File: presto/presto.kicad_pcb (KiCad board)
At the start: 2 copper layers, 27 parts, among them J1 Conn_01x03_Pin, J10 Conn_01x03_Pin, J11 Conn_01x03_Socket, J12 Conn_01x03_Socket, J13 Conn_01x03_Socket, J14 Conn_01x03_Socket, J15 Conn_01x03_Socket, J16 Conn_01x03_Socket, J2 Conn_01x03_Pin, J3 Conn_01x03_Pin, J4 Conn_01x03_Pin, J5 Conn_01x03_Pin, J6 Conn_01x03_Pin, J7 Conn_01x03_Pin, J8 Conn_01x03_Pin, J9 Conn_01x03_Pin

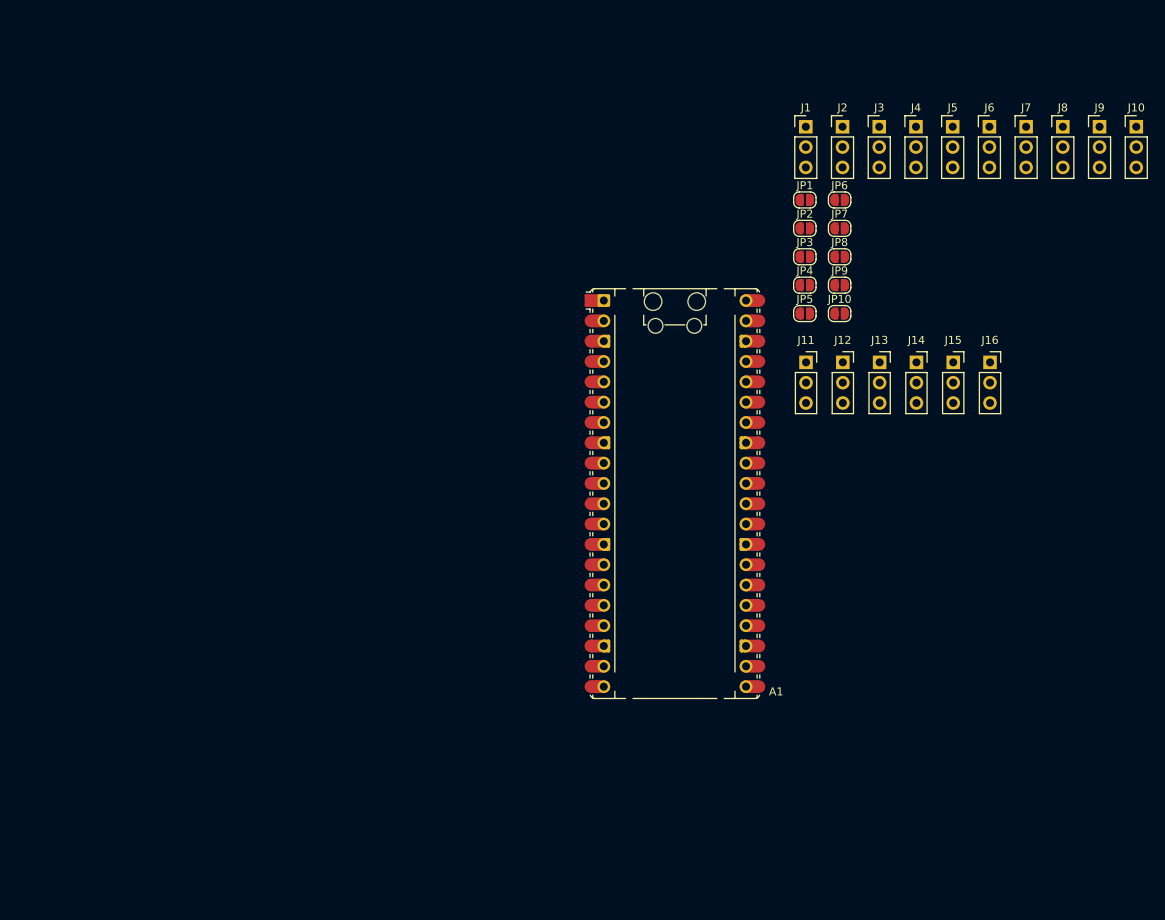
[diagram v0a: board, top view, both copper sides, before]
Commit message: Presto PCB edited with schematic, components placed, wiring in progress
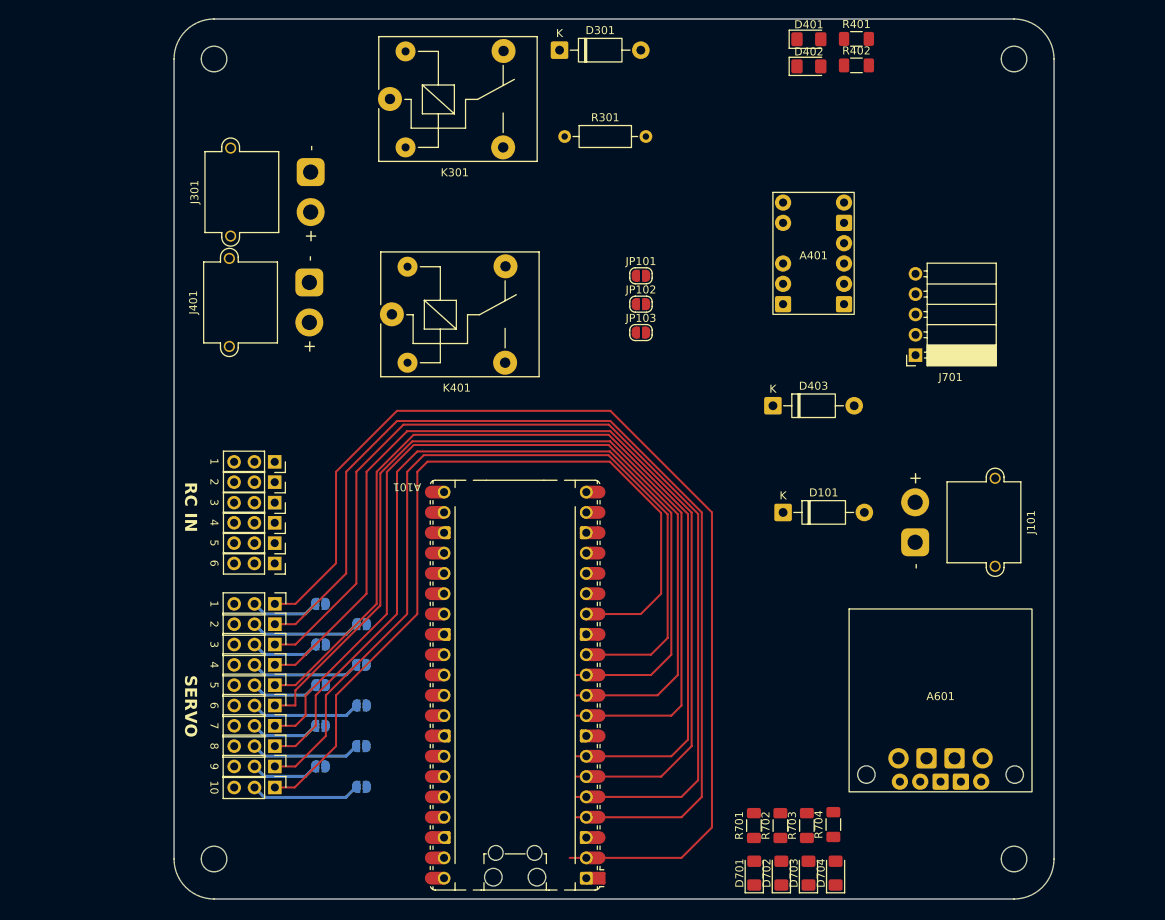
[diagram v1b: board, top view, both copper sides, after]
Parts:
- removed J1, J10, J2, J3, J4, J5, J6, J7, J8, J9: Conn_01x03_Pin, Connector_PinHeader_2.54mm:PinHeader_1x03_P2.54mm_Vertical
- removed JP1, JP10, JP2, JP3, JP4, JP5, JP6, JP7, JP8, JP9: Jumper_2_Small_Open, Jumper:SolderJumper-2_P1.3mm_Open_RoundedPad1.0x1.5mm
- added 1: Conn_01x03_Pin, Connector_PinHeader_2.54mm:PinHeader_1x03_P2.54mm_Vertical, F.Cu at (87.6, 118.1)
- added 10: Conn_01x03_Pin, Connector_PinHeader_2.54mm:PinHeader_1x03_P2.54mm_Vertical, F.Cu at (87.6, 141.1)
- added 2: Conn_01x03_Pin, Connector_PinHeader_2.54mm:PinHeader_1x03_P2.54mm_Vertical, F.Cu at (87.6, 120.7)
- added 3: Conn_01x03_Pin, Connector_PinHeader_2.54mm:PinHeader_1x03_P2.54mm_Vertical, F.Cu at (87.6, 123.2)
- added 4: Conn_01x03_Pin, Connector_PinHeader_2.54mm:PinHeader_1x03_P2.54mm_Vertical, F.Cu at (87.6, 125.7)
- added 5: Conn_01x03_Pin, Connector_PinHeader_2.54mm:PinHeader_1x03_P2.54mm_Vertical, F.Cu at (87.6, 128.3)
- added 6: Conn_01x03_Pin, Connector_PinHeader_2.54mm:PinHeader_1x03_P2.54mm_Vertical, F.Cu at (87.6, 130.8)
- added 7: Conn_01x03_Pin, Connector_PinHeader_2.54mm:PinHeader_1x03_P2.54mm_Vertical, F.Cu at (87.6, 133.3)
- added 8: Conn_01x03_Pin, Connector_PinHeader_2.54mm:PinHeader_1x03_P2.54mm_Vertical, F.Cu at (87.6, 135.9)
- added 9: Conn_01x03_Pin, Connector_PinHeader_2.54mm:PinHeader_1x03_P2.54mm_Vertical, F.Cu at (87.6, 138.4)
- added A401: Pololu RC Switch, GTMRG_Footprints:Pololu_2802_RCSw, F.Cu at (154.9, 76.8)
- added A601: Pololu 5V 3A Regulator S13V30F5, GTMRG_Footprints:Pololu_S13V30F5, F.Cu at (170.8, 130.2)
- added D101: 1N5817, Diode_THT:D_DO-41_SOD81_P10.16mm_Horizontal, F.Cu at (151.1, 106.7)
- added D301: 1N4001, Diode_THT:D_DO-41_SOD81_P10.16mm_Horizontal, F.Cu at (123.2, 48.9)
- added D401: LED, LED_SMD:LED_1206_3216Metric_Pad1.42x1.75mm_HandSolder, F.Cu at (154.4, 47.5)
- added D402: LED, LED_SMD:LED_1206_3216Metric_Pad1.42x1.75mm_HandSolder, F.Cu at (154.4, 50.9)
- added D403: 1N4001, Diode_THT:D_DO-41_SOD81_P10.16mm_Horizontal, F.Cu at (149.9, 93.3)
- added D701: LED, LED_SMD:LED_1206_3216Metric_Pad1.42x1.75mm_HandSolder, F.Cu at (147.5, 151.8)
- added D702: LED, LED_SMD:LED_1206_3216Metric_Pad1.42x1.75mm_HandSolder, F.Cu at (150.9, 151.8)
- added D703: LED, LED_SMD:LED_1206_3216Metric_Pad1.42x1.75mm_HandSolder, F.Cu at (154.3, 151.8)
- added D704: LED, LED_SMD:LED_1206_3216Metric_Pad1.42x1.75mm_HandSolder, F.Cu at (157.7, 151.8)
- added J101: 12V IN, Connector_AMASS:AMASS_XT30PW-M_1x02_P2.50mm_Horizontal, F.Cu at (167.6, 110.4)
- added J301: ESTOP IN, Connector_AMASS:AMASS_XT30PW-M_1x02_P2.50mm_Horizontal, F.Cu at (92.1, 64.1)
- added J401: ESTOP SW, Connector_AMASS:AMASS_XT30PW-M_1x02_P2.50mm_Horizontal, F.Cu at (91.9, 77.9)
- added J701: LED Connector, Connector_PinSocket_2.54mm:PinSocket_1x05_P2.54mm_Horizontal, F.Cu at (167.7, 87.0)
- added JP101: ch6 to gpio16, Jumper:SolderJumper-2_P1.3mm_Open_RoundedPad1.0x1.5mm, F.Cu at (133.4, 77.1)
- added JP102: gpio16 to estop, Jumper:SolderJumper-2_P1.3mm_Open_RoundedPad1.0x1.5mm, F.Cu at (133.4, 80.6)
- added JP103: ch6 to estop, Jumper:SolderJumper-2_P1.3mm_Open_RoundedPad1.0x1.5mm, F.Cu at (133.4, 84.2)
- added JP201: Jumper_2_Small_Open, Jumper:SolderJumper-2_P1.3mm_Open_RoundedPad1.0x1.5mm, B.Cu at (93.3, 118.1)
- added JP202: Jumper_2_Small_Open, Jumper:SolderJumper-2_P1.3mm_Open_RoundedPad1.0x1.5mm, B.Cu at (98.4, 120.7)
- added JP203: Jumper_2_Small_Open, Jumper:SolderJumper-2_P1.3mm_Open_RoundedPad1.0x1.5mm, B.Cu at (93.3, 123.2)
- added JP204: Jumper_2_Small_Open, Jumper:SolderJumper-2_P1.3mm_Open_RoundedPad1.0x1.5mm, B.Cu at (98.4, 125.7)
- added JP205: Jumper_2_Small_Open, Jumper:SolderJumper-2_P1.3mm_Open_RoundedPad1.0x1.5mm, B.Cu at (93.3, 128.3)
- added JP206: Jumper_2_Small_Open, Jumper:SolderJumper-2_P1.3mm_Open_RoundedPad1.0x1.5mm, B.Cu at (98.4, 130.8)
- added JP207: Jumper_2_Small_Open, Jumper:SolderJumper-2_P1.3mm_Open_RoundedPad1.0x1.5mm, B.Cu at (93.3, 133.3)
- added JP208: Jumper_2_Small_Open, Jumper:SolderJumper-2_P1.3mm_Open_RoundedPad1.0x1.5mm, B.Cu at (98.4, 135.9)
- added JP209: Jumper_2_Small_Open, Jumper:SolderJumper-2_P1.3mm_Open_RoundedPad1.0x1.5mm, B.Cu at (93.3, 138.4)
- added JP210: Jumper_2_Small_Open, Jumper:SolderJumper-2_P1.3mm_Open_RoundedPad1.0x1.5mm, B.Cu at (98.4, 141.0)
- added K301: 12V SRD Form C, Relay_THT:Relay_SPDT_SANYOU_SRD_Series_Form_C, F.Cu at (102.0, 55.0)
- added K401: 12V SRD Form C, Relay_THT:Relay_SPDT_SANYOU_SRD_Series_Form_C, F.Cu at (102.2, 81.9)
- added R301: 10k, Resistor_THT:R_Axial_DIN0207_L6.3mm_D2.5mm_P10.16mm_Horizontal, F.Cu at (123.8, 59.7)
- added R401: 220, Resistor_SMD:R_1206_3216Metric_Pad1.30x1.75mm_HandSolder, F.Cu at (160.3, 47.5)
- added R402: 220, Resistor_SMD:R_1206_3216Metric_Pad1.30x1.75mm_HandSolder, F.Cu at (160.3, 50.8)
- added R701: 220, Resistor_SMD:R_1206_3216Metric_Pad1.30x1.75mm_HandSolder, F.Cu at (147.5, 145.8)
- added R702: 220, Resistor_SMD:R_1206_3216Metric_Pad1.30x1.75mm_HandSolder, F.Cu at (150.8, 145.8)
- added R703: 220, Resistor_SMD:R_1206_3216Metric_Pad1.30x1.75mm_HandSolder, F.Cu at (154.1, 145.8)
- added R704: 220, Resistor_SMD:R_1206_3216Metric_Pad1.30x1.75mm_HandSolder, F.Cu at (157.4, 145.7)
- added REF**: MountingHole_3.2mm_M3, MountingHole:MountingHole_3.2mm_M3, F.Cu at (80.0, 150.0)
- added REF**: MountingHole_3.2mm_M3, MountingHole:MountingHole_3.2mm_M3, F.Cu at (180.0, 50.0)
- added REF**: MountingHole_3.2mm_M3, MountingHole:MountingHole_3.2mm_M3, F.Cu at (80.0, 50.0)
- added REF**: MountingHole_3.2mm_M3, MountingHole:MountingHole_3.2mm_M3, F.Cu at (180.0, 150.0)
- moved 6 92.9 mm to (87.6, 113.1), turned to -90 degrees
- moved 5 87.8 mm to (87.6, 110.5), turned to -90 degrees
- moved 4 82.7 mm to (87.6, 108.0), turned to -90 degrees
- moved 3 77.6 mm to (87.6, 105.5), turned to -90 degrees
- moved 2 72.6 mm to (87.6, 102.9), turned to -90 degrees
- moved 1 67.6 mm to (87.6, 100.4), turned to -90 degrees
- moved A101 31.2 mm to (117.6, 128.3), turned to 180 degrees
- renumbered J11 to 1, J12 to 2, J13 to 3, J14 to 4, J15 to 5, J16 to 6, A1 to A101
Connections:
- A101 pad 10: unconnected-(A1-GPIO7-Pad10) -> /Servo Interface/servo7
- A101 pad 11: unconnected-(A1-GPIO8-Pad11) -> /Servo Interface/servo8
- A101 pad 12: unconnected-(A1-GPIO9-Pad12) -> /Servo Interface/servo9
- A101 pad 13: Net-(A1-GND-Pad13) -> GND
- A101 pad 14: unconnected-(A1-GPIO10-Pad14) -> /Servo Interface/servo10
- A101 pad 18: Net-(A1-GND-Pad13) -> GND
- A101 pad 2: unconnected-(A1-GPIO1-Pad2) -> /Servo Interface/servo1
- A101 pad 21: /Servo Interface/servo1 -> /gpio16
- A101 pad 22: unconnected-(A1-GPIO17-Pad22) -> /gpio17
- A101 pad 23: Net-(A1-GND-Pad13) -> GND
- A101 pad 24: unconnected-(A1-GPIO18-Pad24) -> /EStop Reading/estop_signal
- A101 pad 25: unconnected-(A1-GPIO19-Pad25) -> /LED Interface/red
- A101 pad 26: unconnected-(A1-GPIO20-Pad26) -> /LED Interface/yellow
- A101 pad 27: unconnected-(A1-GPIO21-Pad27) -> /LED Interface/green
- A101 pad 28: Net-(A1-GND-Pad13) -> GND
- A101 pad 29: unconnected-(A1-GPIO22-Pad29) -> /LED Interface/blue
- A101 pad 3: Net-(A1-GND-Pad13) -> GND
- A101 pad 36: unconnected-(A1-3V3-Pad36) -> +3V3
- A101 pad 38: Net-(A1-GND-Pad13) -> GND
- A101 pad 39: unconnected-(A1-VSYS-Pad39) -> +5V
- A101 pad 4: unconnected-(A1-GPIO2-Pad4) -> /Servo Interface/servo2
- A101 pad 5: unconnected-(A1-GPIO3-Pad5) -> /Servo Interface/servo3
- A101 pad 6: unconnected-(A1-GPIO4-Pad6) -> /Servo Interface/servo4
- A101 pad 7: unconnected-(A1-GPIO5-Pad7) -> /Servo Interface/servo5
- A101 pad 8: Net-(A1-GND-Pad13) -> GND
- A101 pad 9: unconnected-(A1-GPIO6-Pad9) -> /Servo Interface/servo6
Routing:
- net /Servo Interface/servo1: track 0.00 -> 135.3 mm
- net /Servo Interface/servo2: track 0.00 -> 128.4 mm
- net /Servo Interface/servo3: track 0.00 -> 126.5 mm
- net /Servo Interface/servo4: track 0.00 -> 122.6 mm
- net /Servo Interface/servo5: track 0.00 -> 121.4 mm
- net /Servo Interface/servo6: track 0.00 -> 116.8 mm
- net /Servo Interface/servo7: track 0.00 -> 114.3 mm
- net /Servo Interface/servo8: track 0.00 -> 111.3 mm
- net /Servo Interface/servo9: track 0.00 -> 107.4 mm
- net /Servo Interface/servo10: track 0.00 -> 101.7 mm
- net Net-(J210-Pin_2): track 0.00 -> 13.8 mm
- net Net-(J206-Pin_2): track 0.00 -> 13.8 mm
- net Net-(J202-Pin_2): track 0.00 -> 13.8 mm
- net Net-(J208-Pin_2): track 0.00 -> 13.7 mm
- net Net-(J204-Pin_2): track 0.00 -> 13.7 mm
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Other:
- board outline added: 110 x 110 mm
- board text added: "RC IN"
- board text added: "SERVO"

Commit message: Presto PCB all wired up, please let me know if any changes are necessary
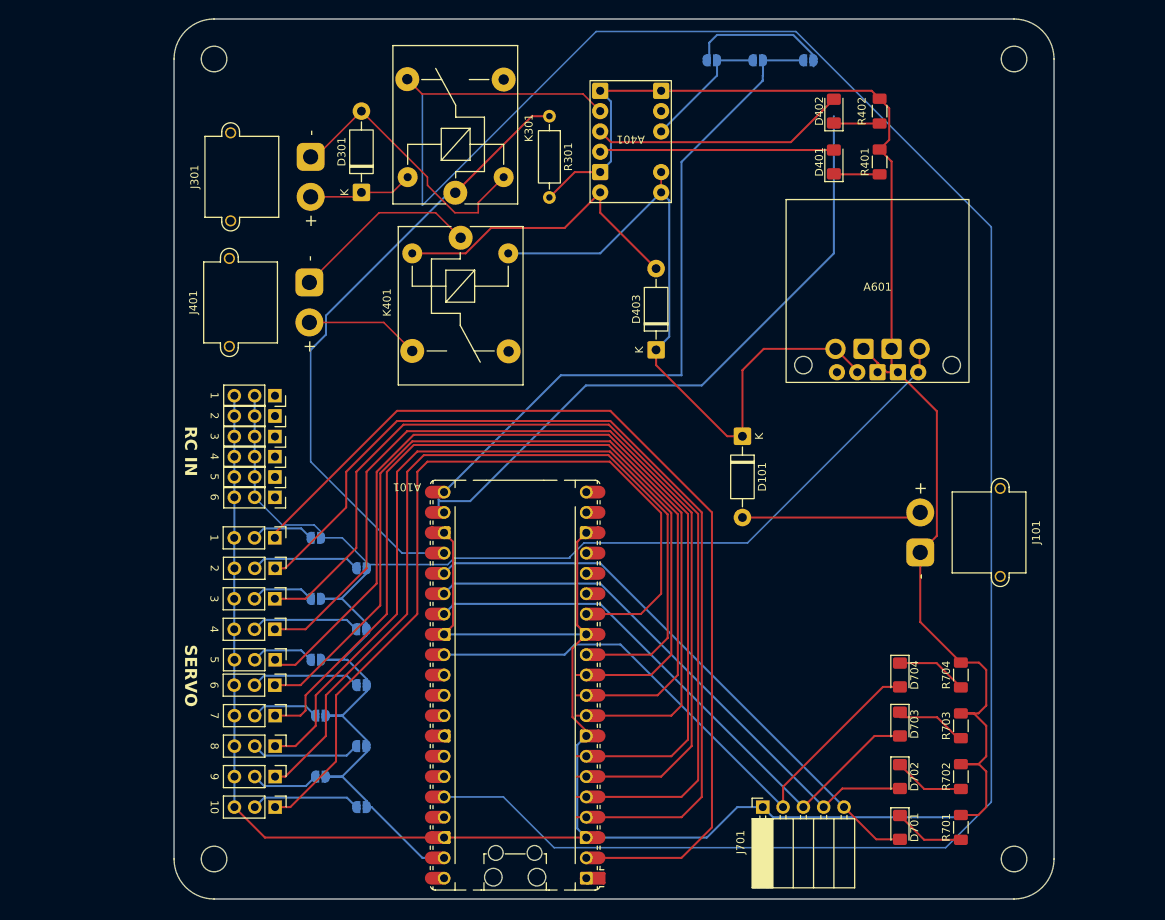
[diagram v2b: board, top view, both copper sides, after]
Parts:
- JP101, JP102, JP103: moved to B.Cu
- moved J701 59.6 mm to (148.6, 143.5), turned to 90 degrees
- moved A601 51.8 mm to (162.9, 79.0)
- moved JP103 35.2 mm to (142.2, 50.2)
- moved JP101 34.1 mm to (154.3, 50.2), turned to 180 degrees
- moved JP102 33.8 mm to (148.0, 50.2), turned to 180 degrees
- moved D301 30.5 mm to (98.4, 66.7), turned to 90 degrees
- moved A401 29.8 mm to (132.1, 57.8), turned to 180 degrees
- moved D704 26.0 mm to (165.7, 127.0), turned to -90 degrees
- moved R701 25.9 mm to (173.4, 146.1)
- moved R704 24.6 mm to (173.4, 127.0)
- moved R702 23.4 mm to (173.4, 139.7)
- moved R703 22.9 mm to (173.4, 133.3)
- moved D703 21.9 mm to (165.7, 133.1), turned to -90 degrees
- moved D702 19.1 mm to (165.7, 139.7), turned to -90 degrees
- moved D701 19.1 mm to (165.7, 146.1), turned to -90 degrees
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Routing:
- net GND: track 0.00 -> 396.0 mm
- net +3V3: track 0.00 -> 277.8 mm
- net +5V: track 0.00 -> 186.2 mm
- net /gpio17: track 0.00 -> 113.4 mm
- net +12V: track 0.00 -> 87.0 mm
- net /gpio16: track 0.00 -> 84.4 mm
- net /EStop Reading/estop_signal: track 0.00 -> 79.6 mm
- net /LED Interface/blue: track 0.00 -> 73.6 mm
- net /LED Interface/green: track 0.00 -> 71.8 mm
- net /LED Interface/red: track 0.00 -> 71.8 mm
- net /LED Interface/yellow: track 0.00 -> 70.1 mm
- net /EStop Trigger/LOAD_LO: track 0.00 -> 39.1 mm
- net Net-(D301-A): track 0.00 -> 34.9 mm
- net Net-(A401-GOOD): track 0.00 -> 29.3 mm
- net Net-(J401-Pin_1): track 0.00 -> 23.8 mm
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
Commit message: Presto PCB wired up with most changes implemented + filled zone
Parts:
- added ?: , , F.Cu at (180.0, 50.0)
- added REF**: MountingHole_2.5mm, MountingHole:MountingHole_2.5mm, F.Cu at (179.7, 88.3)
- added REF**: MountingHole_2.5mm, MountingHole:MountingHole_2.5mm, F.Cu at (179.8, 70.5)
- REF** (x4): value MountingHole_3.2mm_M3 -> MountingHole_2.5mm; footprint MountingHole:MountingHole_3.2mm_M3 -> MountingHole:MountingHole_2.5mm
- moved R701 27.1 mm to (146.5, 142.9), turned to 0 degrees
- moved J701 26.2 mm to (172.7, 133.3), turned to 180 degrees
- moved D701 22.1 mm to (146.5, 135.3), turned to 180 degrees
- moved R702 20.4 mm to (153.2, 142.9), turned to 0 degrees
- moved R704 16.8 mm to (167.1, 142.6), turned to 0 degrees
- moved R703 16.1 mm to (160.2, 142.6), turned to 0 degrees
- moved D702 12.9 mm to (153.7, 135.3), turned to 180 degrees
- moved D704 8.13 mm to (167.1, 135.0), turned to 180 degrees
- moved D703 5.68 mm to (160.4, 135.0), turned to 180 degrees
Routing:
- net GND: track 396.0 -> 5.62 mm
- net +3V3: track 277.8 -> 221.4 mm
- net /gpio17: track 113.4 -> 92.1 mm
- net /LED Interface/yellow: track 70.1 -> 83.7 mm
- net /LED Interface/green: track 71.8 -> 83.4 mm
- net /LED Interface/red: track 71.8 -> 77.4 mm
- net /LED Interface/blue: track 73.6 -> 78.3 mm
- net /Servo Interface/servo7: track 113.3 -> 111.3 mm
- net /Servo Interface/servo6: track 114.6 -> 112.5 mm
- net /Servo Interface/servo3: track 121.5 -> 119.5 mm
- net /Servo Interface/servo8: track 111.3 -> 109.3 mm
- net /Servo Interface/servo4: track 118.9 -> 116.8 mm
- net /Servo Interface/servo5: track 118.9 -> 116.8 mm
- net /Servo Interface/servo2: track 120.6 -> 119.4 mm
- net Net-(JP101-A): track 17.8 -> 16.8 mm
- added copper zone on F.Cu, net GND
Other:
- board text added: "6 mm apart"
